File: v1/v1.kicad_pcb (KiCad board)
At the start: 2 copper layers, 101.5 x 105.4 mm, 63 parts, among them CON1 SNES-CONN

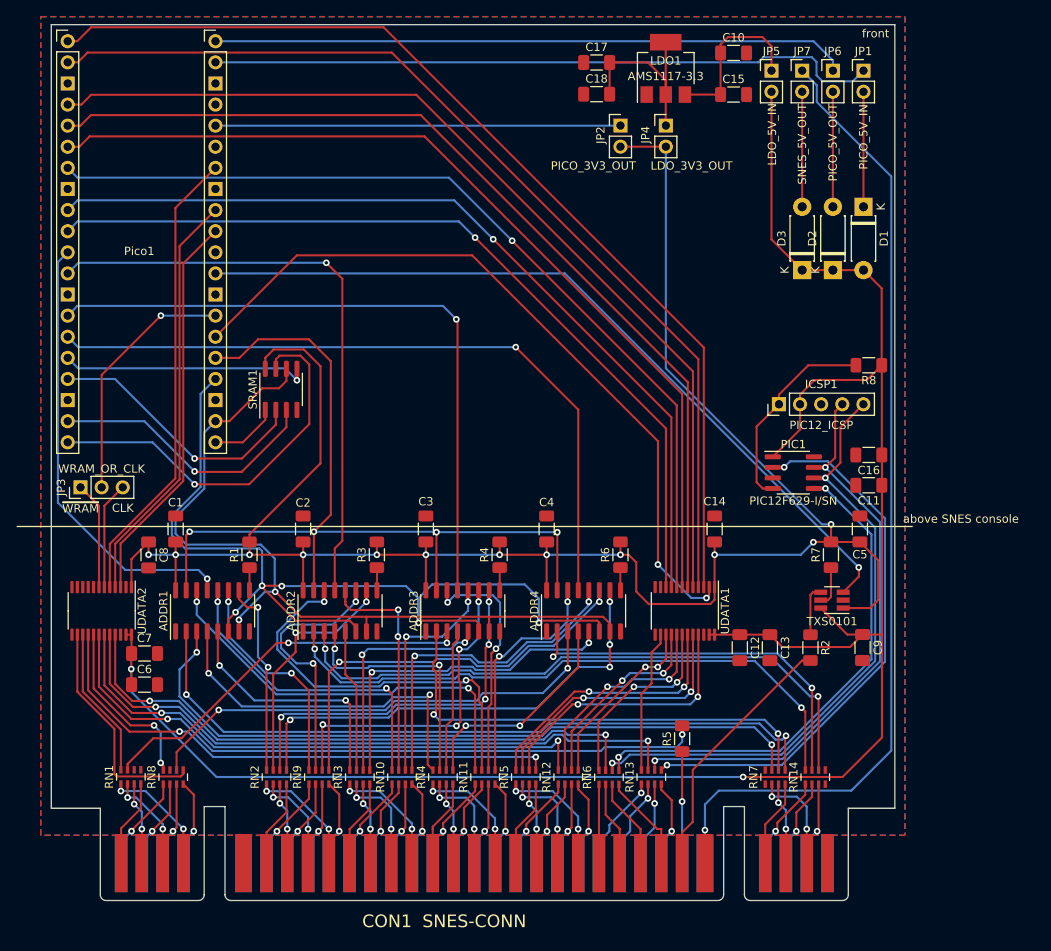
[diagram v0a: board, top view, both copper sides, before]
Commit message: v1: increase 5V traces to 0.5mm; add renders
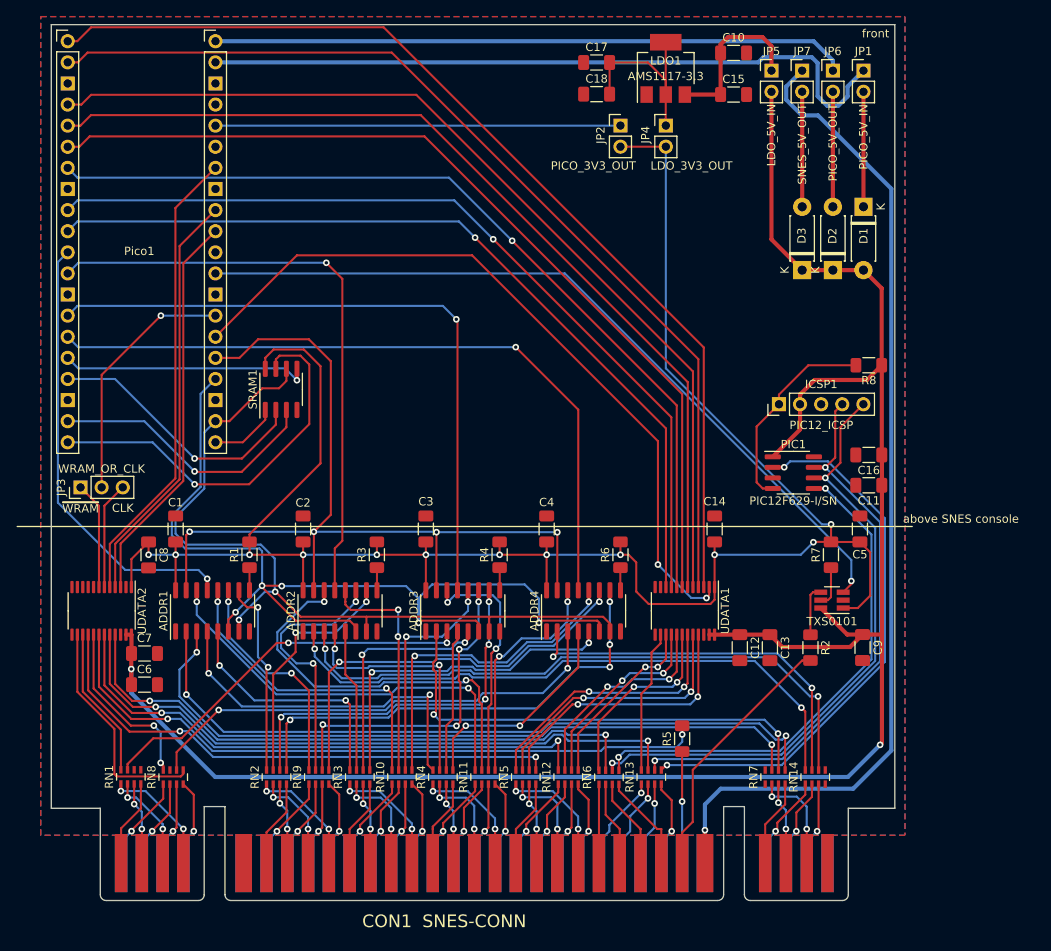
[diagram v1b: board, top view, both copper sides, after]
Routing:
- net Net-(JP1-Pad1): track 80.9 -> 85.4 mm
- net Net-(CON1-Pad27): track 122.4 -> 125.1 mm
- net +3.3V: track 243.5 -> 241.8 mm
- net /~{RESET}: track 95.8 -> 95.1 mm

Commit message: v1: updated footprint of RPi Pico to include pin labels; added test points for power rails
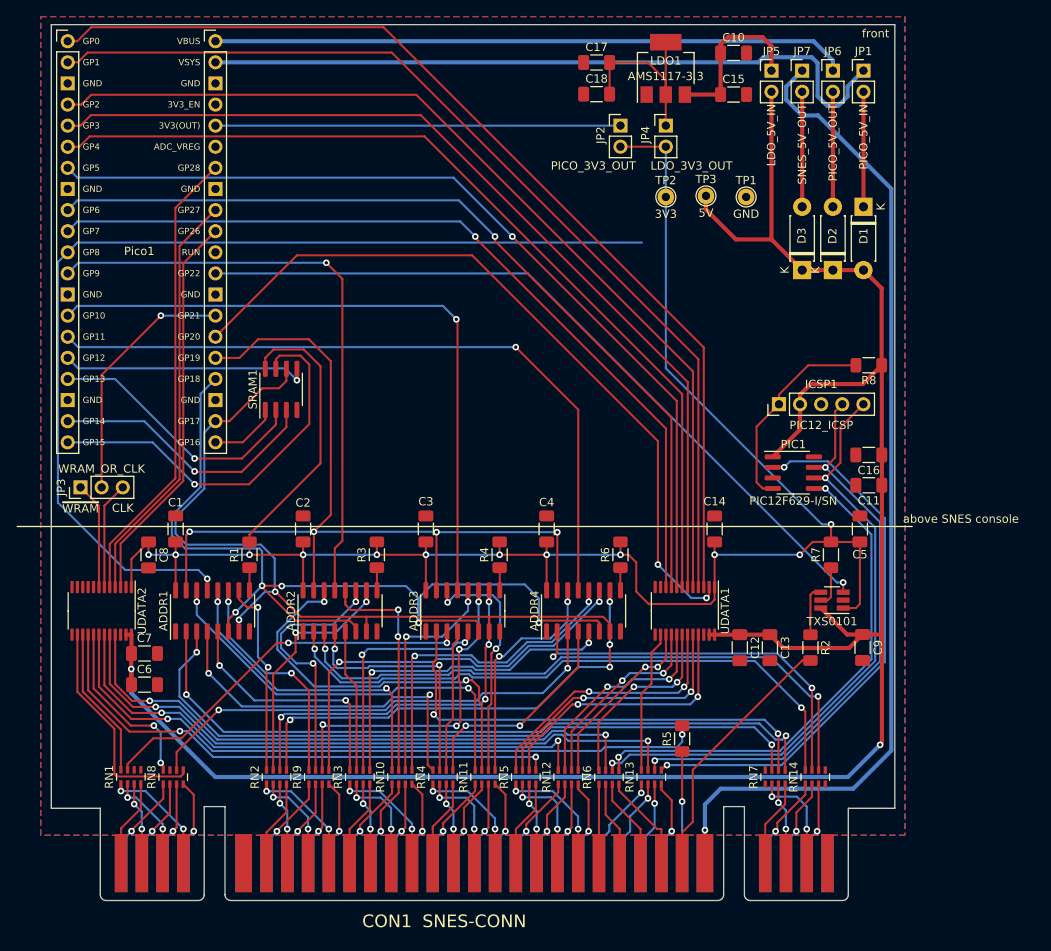
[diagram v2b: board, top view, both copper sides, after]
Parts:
- added TP1: GND, TestPoint:TestPoint_THTPad_D2.0mm_Drill1.0mm, F.Cu at (169.9, 49.2)
- added TP2: 3V3, TestPoint:TestPoint_THTPad_D2.0mm_Drill1.0mm, F.Cu at (160.2, 49.2)
- added TP3: 5V, TestPoint:TestPoint_THTPad_D2.0mm_Drill1.0mm, F.Cu at (165.1, 49.1)
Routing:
- net /ADDR1QH: track 53.8 -> 123.3 mm
- net +5V: track 242.1 -> 253.2 mm
- net /~{RESET}: track 95.1 -> 92.1 mm
- net +3.3V: track 241.8 -> 240.6 mm

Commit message: v1: added LCSC part numbers; switched out diodes for SMT; 74LV166A is out of stock at LCSC so need to replace it
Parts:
- D1, D2, D3: footprint Diode_THT:D_DO-41_SOD81_P7.62mm_Horizontal -> Diode_SMD:D_SMA_Handsoldering
- moved D1 5.12 mm to (184.0, 55.5)
- moved D2 2.50 mm to (180.3, 55.5)
- moved D3 2.50 mm to (176.6, 55.5)
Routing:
- net /ADDR1QH: track 123.3 -> 53.8 mm
- net Net-(D2-Pad2): track 13.8 -> 16.5 mm
- net Net-(D3-Pad2): track 13.8 -> 16.5 mm
- net Net-(D1-Pad1): track 13.8 -> 16.5 mm
- net /YA20: track 50.1 -> 48.4 mm
- net /YA0: track 43.4 -> 41.7 mm
- net /YPA3: track 46.1 -> 44.8 mm
- net /Y~{CE}: track 67.6 -> 66.3 mm
- net /YA21: track 47.5 -> 46.2 mm
- net /YA19: track 39.8 -> 38.9 mm
- net /YPA0: track 87.2 -> 88.0 mm
- net /YA15: track 49.9 -> 49.2 mm
- net /YA4: track 29.7 -> 30.4 mm
- net /YCPU_CLK: track 82.0 -> 82.6 mm
- net /YPA4: track 86.3 -> 86.8 mm

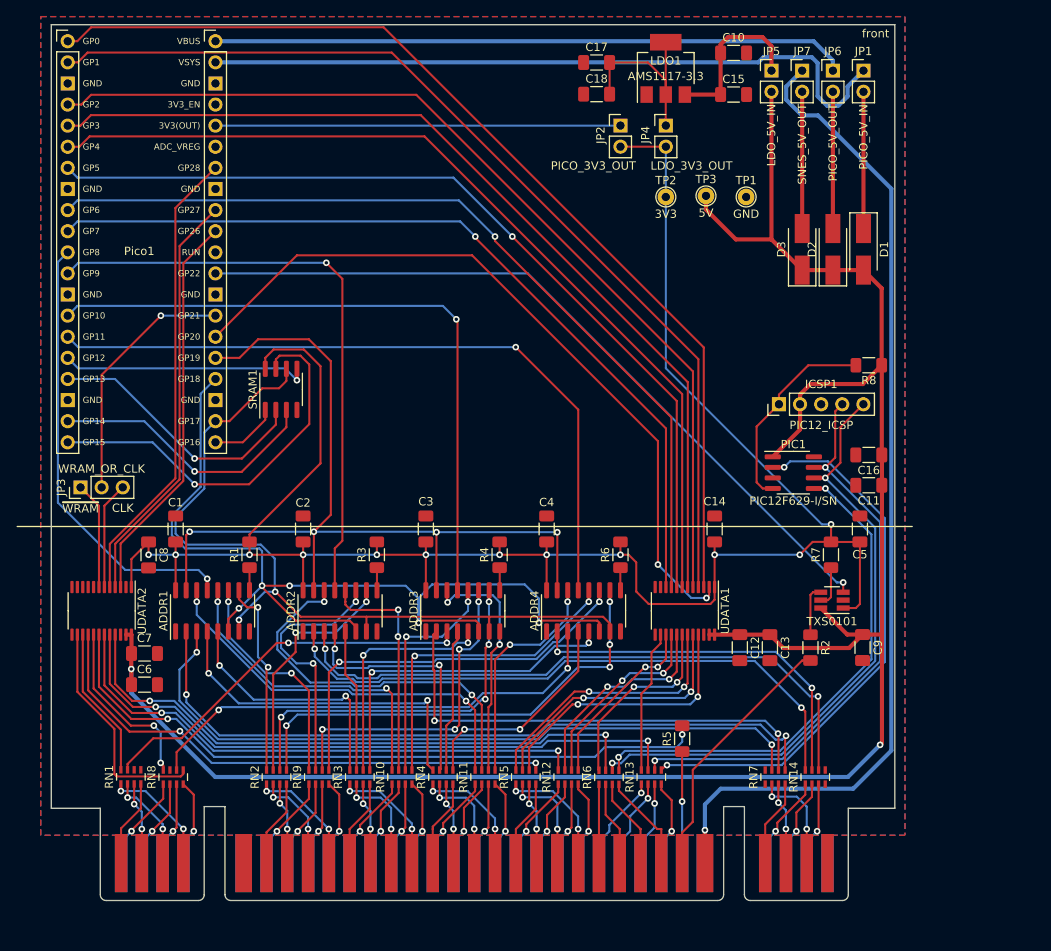
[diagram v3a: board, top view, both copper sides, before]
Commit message: v1: restarting routing of shift registers in new orientation with replacement components
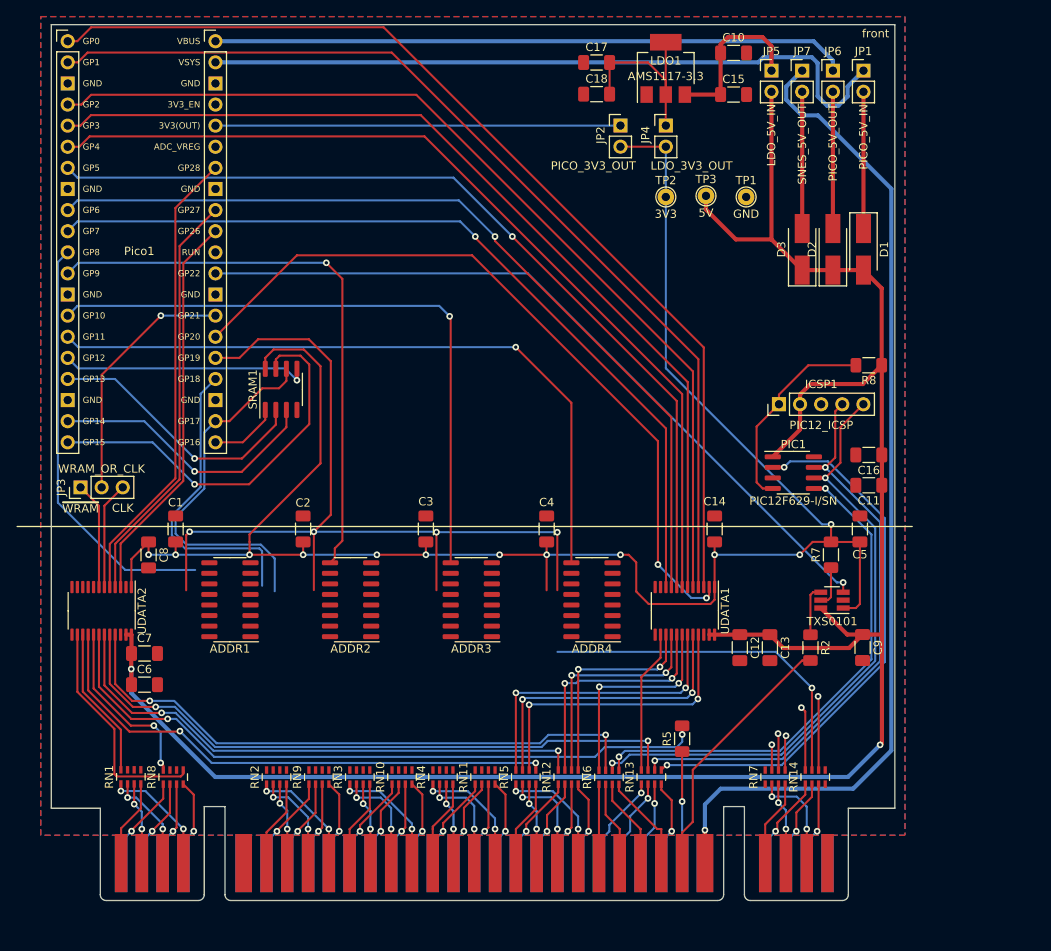
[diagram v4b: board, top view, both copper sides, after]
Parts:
- removed R1, R3, R4, R6: 10kR, Resistor_SMD:R_1206_3216Metric_Pad1.30x1.75mm_HandSolder
- ADDR1, ADDR2, ADDR3, ADDR4: value 74LV166A -> 74LV165D,118
- moved ADDR1 2.48 mm to (107.8, 97.7), turned to 180 degrees
- moved ADDR2 1.85 mm to (122.3, 97.7), turned to 180 degrees
- moved ADDR3 1.68 mm to (136.8, 97.7), turned to 180 degrees
- moved ADDR4 1.68 mm to (151.3, 97.7), turned to 180 degrees
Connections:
- ADDR1 pad 1: GND -> /~{ADDRLD}
- ADDR1 pad 10: /YA8 -> GND
- ADDR1 pad 11: /YA12 -> /YPA0
- ADDR1 pad 12: /YA16 -> /YPA4
- ADDR1 pad 13: /ADDR1QH -> /YA0
- ADDR1 pad 14: /YA20 -> /YA4
- ADDR1 pad 15: /~{ADDRLD} -> /CLK_INH
- ADDR1 pad 2: /YPA0 -> /CLK_133MHZ
- ADDR1 pad 3: /YPA4 -> /YA8
- ADDR1 pad 4: /YA0 -> /YA12
- ADDR1 pad 5: /YA4 -> /YA16
- ADDR1 pad 6: /CLK_INH -> /YA20
- ADDR1 pad 7: /CLK_133MHZ -> unconnected-(ADDR1-Pad7)
- ADDR1 pad 9: Net-(ADDR1-Pad9) -> /ADDR1QH
- ADDR2 pad 1: GND -> /~{ADDRLD}
- ADDR2 pad 10: /YA9 -> GND
- ADDR2 pad 11: /YA13 -> /YPA1
- ADDR2 pad 12: /YA17 -> /YPA5
- ADDR2 pad 13: /ADDR2QH -> /YA1
- ADDR2 pad 14: /YA21 -> /YA5
- ADDR2 pad 15: /~{ADDRLD} -> /CLK_INH
- ADDR2 pad 2: /YPA1 -> /CLK_133MHZ
- ADDR2 pad 3: /YPA5 -> /YA9
- ADDR2 pad 4: /YA1 -> /YA13
- ADDR2 pad 5: /YA5 -> /YA17
- ADDR2 pad 6: /CLK_INH -> /YA21
- ADDR2 pad 7: /CLK_133MHZ -> unconnected-(ADDR2-Pad7)
- ADDR2 pad 9: Net-(ADDR2-Pad9) -> /ADDR2QH
- ADDR3 pad 1: GND -> /~{ADDRLD}
- ADDR3 pad 10: /YA10 -> GND
- ADDR3 pad 11: /YA14 -> /YPA2
- ADDR3 pad 12: /YA18 -> /YPA6
- ADDR3 pad 13: /ADDR3QH -> /YA2
- ADDR3 pad 14: /YA22 -> /YA6
- ADDR3 pad 15: /~{ADDRLD} -> /CLK_INH
- ADDR3 pad 2: /YPA2 -> /CLK_133MHZ
- ADDR3 pad 3: /YPA6 -> /YA10
- ADDR3 pad 4: /YA2 -> /YA14
- ADDR3 pad 5: /YA6 -> /YA18
- ADDR3 pad 6: /CLK_INH -> /YA22
- ADDR3 pad 7: /CLK_133MHZ -> unconnected-(ADDR3-Pad7)
- ADDR3 pad 9: Net-(ADDR3-Pad9) -> /ADDR3QH
- ADDR4 pad 1: GND -> /~{ADDRLD}
- ADDR4 pad 10: /YA11 -> GND
- ADDR4 pad 11: /YA15 -> /YPA3
- ADDR4 pad 12: /YA19 -> /YPA7
- ADDR4 pad 13: /ADDR4QH -> /YA3
- ADDR4 pad 14: /YA23 -> /YA7
- ADDR4 pad 15: /~{ADDRLD} -> /CLK_INH
- ADDR4 pad 2: /YPA3 -> /CLK_133MHZ
- ADDR4 pad 3: /YPA7 -> /YA11
- ADDR4 pad 4: /YA3 -> /YA15
- ADDR4 pad 5: /YA7 -> /YA19
- ADDR4 pad 6: /CLK_INH -> /YA23
- ADDR4 pad 7: /CLK_133MHZ -> unconnected-(ADDR4-Pad7)
- ADDR4 pad 9: Net-(ADDR4-Pad9) -> /ADDR4QH
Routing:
- net /YPA0: track 88.0 -> 4.17 mm, vias 2 -> 1
- net /YPA4: track 86.8 -> 3.05 mm, vias 2 -> 1
- net /CLK_INH: track 118.6 -> 36.8 mm, vias 5 -> 0
- net /YPA5: track 75.7 -> 8.88 mm, vias 2 -> 1
- net /YPA1: track 74.0 -> 7.69 mm, vias 2 -> 1
- net /YPA7: track 57.8 -> 0.00 mm, vias 2 -> 0
- net /YA11: track 56.4 -> 0.00 mm, vias 4 -> 0
- net /CLK_133MHZ: track 98.4 -> 44.6 mm, vias 2 -> 0
- net /YPA2: track 57.3 -> 4.40 mm, vias 2 -> 1
- net /YA15: track 49.2 -> 0.00 mm, vias 2 -> 0
- net /YA20: track 48.4 -> 0.00 mm, vias 2 -> 0
- net /YPA6: track 46.5 -> 0.00 mm, vias 2 -> 0
- net /YA21: track 46.2 -> 0.00 mm, vias 2 -> 0
- net /YA10: track 45.2 -> 0.00 mm, vias 4 -> 0
- net /YA0: track 41.7 -> 0.00 mm, vias 2 -> 0
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
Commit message: v1: switched back to TSSOP-16 package shift register for better switching characteristics; routed entire pcb
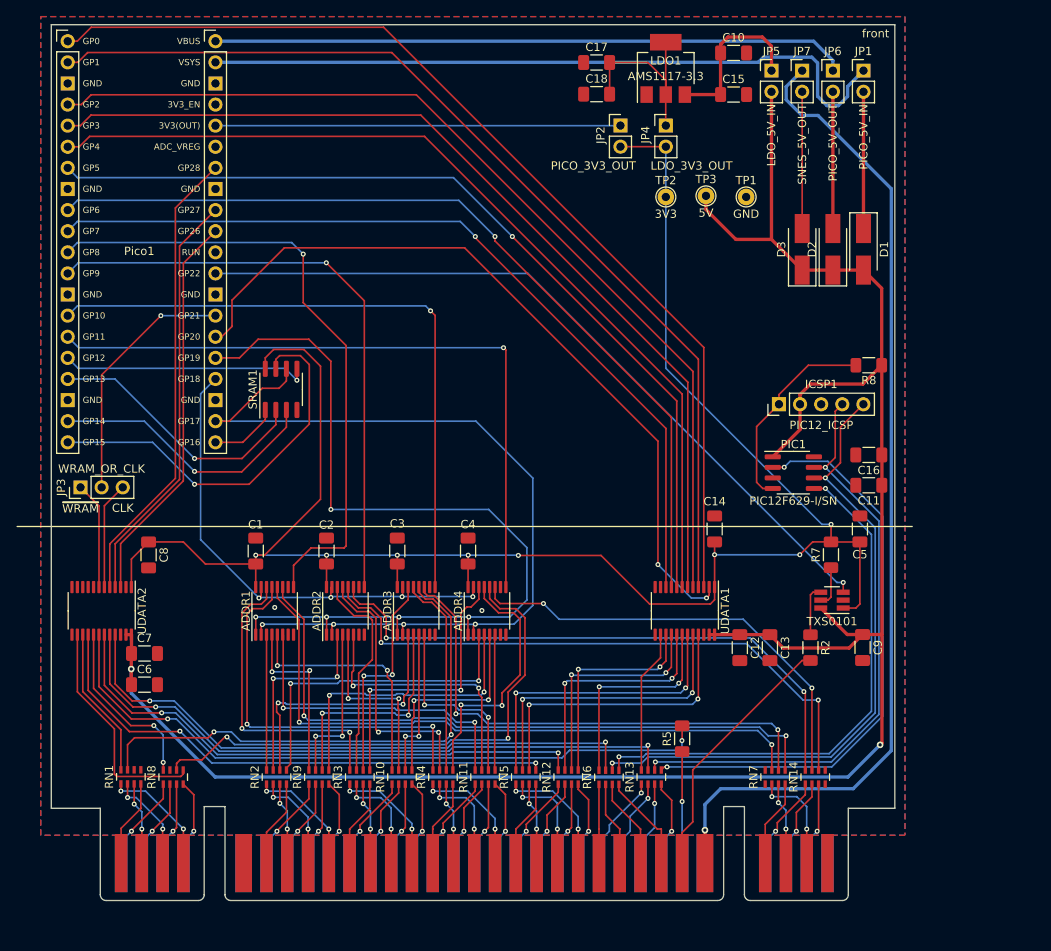
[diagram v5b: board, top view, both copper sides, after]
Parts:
- ADDR1, ADDR2, ADDR3, ADDR4: value 74LV165D,118 -> SN74LV165APWR; footprint Package_SO:SOIC-16_3.9x9.9mm_P1.27mm -> Package_SO:TSSOP-16_4.4x5mm_P0.65mm
- moved ADDR4 12.7 mm to (138.7, 99.0), turned to 90 degrees
- moved C1 10.00 mm to (110.9, 91.8)
- moved C4 9.82 mm to (136.4, 91.8)
- moved ADDR3 6.76 mm to (130.2, 99.0), turned to 90 degrees
- moved ADDR1 5.54 mm to (113.2, 99.0), turned to 90 degrees
- moved C3 4.34 mm to (127.9, 91.8)
- moved C2 3.87 mm to (119.4, 91.8)
- moved ADDR2 1.48 mm to (121.7, 99.0), turned to 90 degrees
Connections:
- net /CLK_INH renamed /~{ADDRCE}
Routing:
- net /YPA0: track 4.17 -> 79.9 mm, vias 1 -> 2
- net /YPA4: track 3.05 -> 78.6 mm, vias 1 -> 2
- net /YPA7: track 0.00 -> 64.6 mm, vias 0 -> 2
- net /YPA5: track 8.88 -> 73.1 mm, vias 1 -> 2
- net /YPA1: track 7.69 -> 71.1 mm, vias 1 -> 2
- net /YPA6: track 0.00 -> 63.3 mm, vias 0 -> 2
- net /CLK_133MHZ: track 44.6 -> 107.1 mm, vias 0 -> 4
- net /YPA2: track 4.40 -> 61.7 mm, vias 1 -> 2
- net /YA0: track 0.00 -> 46.3 mm, vias 0 -> 2
- net /YA11: track 0.00 -> 38.7 mm, vias 0 -> 2
- net /YA20: track 0.00 -> 38.3 mm, vias 0 -> 2
- net /YA4: track 0.00 -> 36.7 mm, vias 0 -> 2
- net /YA15: track 0.00 -> 35.0 mm, vias 0 -> 2
- net /YA7: track 0.00 -> 34.2 mm, vias 0 -> 2
- net /YA10: track 0.00 -> 32.1 mm, vias 0 -> 2
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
